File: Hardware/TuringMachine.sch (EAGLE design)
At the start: 79 parts, among them IC1 TL072, IC2 4015, IC3 4015, IC4 TL074, IC5 4016, T1 2N3904, T2 2N3904, T3 2N3904

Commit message: Hand routing
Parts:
- removed 78L09: (no value), v-reg:78LXX
- removed IC4: TL074, linear:TL074P
- added C17: 1n, TomW:C-EU050-024X044
- added C18: 0.47uf, rcl:C-EU050-035X075
- added IC6, IC7: TL072P, TomW:TL072P
- added R20: 3.3k, TomW:R-EU_0207/7
- added TL431: (no value), TomW:TL431CLP
- C12: value 100n -> 1n
- IC1: value TL072 -> TL072P
- R26: value 10k -> 5.1k
- R27, R28: value 10k -> 1.6k
- R3: value 100k -> 68k
- R7: value 1m -> 470k
- renumbered ADD_0_1 to WRITE
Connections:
- removed net N$38: 78L09.OUT, R28.1
- new net N$18: R20.1, R28.1, TL431.C, TL431.R
- new net N$9: C18.1, R32.1
- net +12V: now also IC6P.V+, IC7P.V+, R1.1, R20.2, R23.1; no longer 78L09.IN, C12.1, IC4P.V+, R1.2, R23.2
- net -12V: now also IC6P.V-, IC7P.V-, R35.1; no longer IC4P.V-, R35.2
- net B1: now also R14.2; no longer R14.1
- net END_OF_LOOP: now also IC5A.A, R4.1; no longer IC5D.A, R4.2
- net GND: now also C1.1, C15.1, C3.1, IC5C.C, IC5D.C, IC6A.+IN, IC7A.+IN, R27.1, TL431.A; no longer 78L09.GND, C1.2, C12.2, C15.2, C3.2, IC4A.+IN, IC4C.+IN, IC5A.C, IC5B.C, R27.2
- net MAIN_OUT: now also C17.2, IC7A.OUT; no longer IC4A.OUT
- net N$1: now also R4.2; no longer R4.1
- net N$10: now also C1.2; no longer C1.1
- net N$11: now also R18.1; no longer R18.2
- net N$12: now also IC7B.-IN; no longer IC4B.-IN
- net N$13: now also C17.1, IC7A.-IN; no longer IC4A.-IN
- net N$16: now also C10.1; no longer C10.2
- net N$19: now also R18.2; no longer R18.1
- net N$20: now also C10.2, R30.1; no longer C10.1, R30.2
- net N$21: now also R30.2, R31.2; no longer R30.1, R31.1
- net N$22: now also C18.2, R31.1; no longer R31.2, R32.2
- net N$23: now also R27.2; no longer R27.1
- net N$24: now also IC5A.C, IC6B.OUT, R25.1; no longer IC4D.OUT, IC5D.C, R25.2
- net N$27: now also C12.1, R32.2; no longer R32.1
- net N$28: now also R14.1; no longer R14.2
- net N$4: now also IC5B.A, R1.2; no longer IC5C.A, R1.1
- net N$41: now also C11.1, C12.2; no longer C11.2
- net N$44: now also R25.2; no longer R25.1
- net N$45: now also IC5B.C; no longer IC5C.C
- net N$47: now also R23.2; no longer R23.1
- net N$48: now also R35.2; no longer R35.1
- net N$5: now also C15.2, IC7B.+IN; no longer C15.1, IC4B.+IN
- net N$6: now also IC6A.-IN; no longer IC4C.-IN
- net N$7: now also IC6A.OUT, IC6B.-IN; no longer IC4C.OUT, IC4D.-IN
- net N$8: now also IC7B.OUT; no longer IC4B.OUT
- net NOISE: now also C11.2, IC6B.+IN; no longer C11.1, IC4D.+IN
- net START_OF_LOOP: now also IC5A.B, IC5B.B; no longer IC5C.B, IC5D.B
- net STEP_12: now also C3.2; no longer C3.1
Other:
- moved on the sheet: C10, C12, C13, C14, C5, C6, C7, C8, EXPANSION, IC1A, IC2P, IC3P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

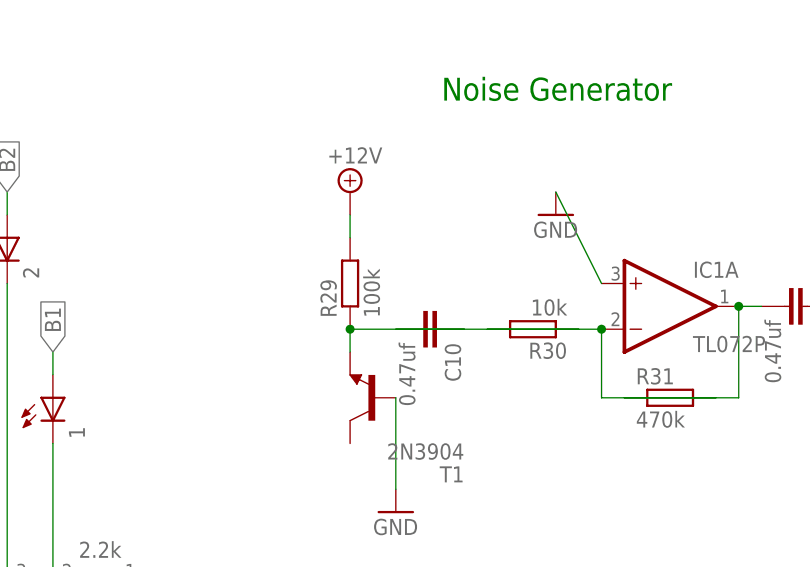
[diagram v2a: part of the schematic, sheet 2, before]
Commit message: manual routing
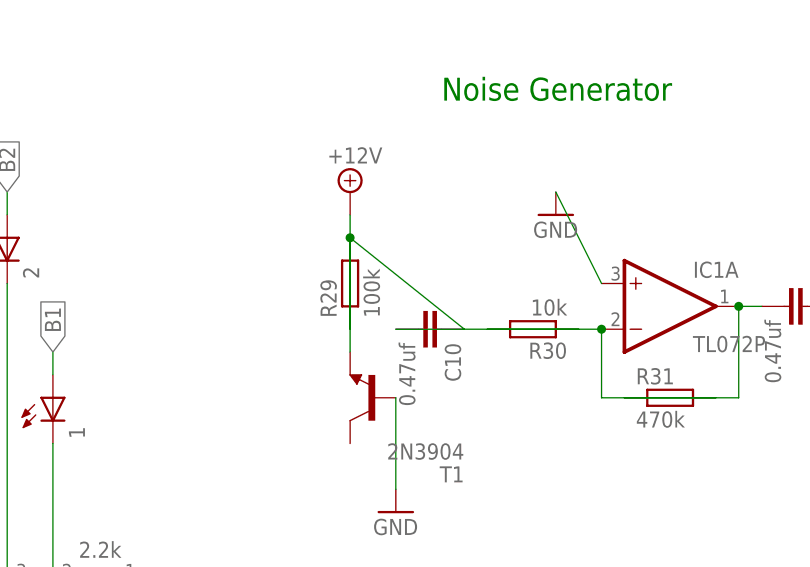
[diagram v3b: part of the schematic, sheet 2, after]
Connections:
- net +12V: now also R29.1; no longer R29.2
- net N$16: now also R29.2; no longer R29.1
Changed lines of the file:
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@@
 </segment>
 <segment>
-<pinref part="R29" gate="G$1" pin="2"/>
+<pinref part="R29" gate="G$1" pin="1"/>
 <pinref part="P+13" gate="+12V" pin="+12V"/>
-<wire x1="142.24" y1="91.44" x2="142.24" y2="88.9" width="0.1524" layer="91"/>
+<wire x1="142.24" y1="91.44" x2="142.24" y2="78.74" width="0.1524" layer="91"/>
 </segment>
 <segment>
@@
 <segment>
 <pinref part="T1" gate="G1" pin="E"/>
-<pinref part="R29" gate="G$1" pin="1"/>
-<wire x1="142.24" y1="76.2" x2="142.24" y2="78.74" width="0.1524" layer="91"/>
+<pinref part="R29" gate="G$1" pin="2"/>
+<wire x1="142.24" y1="76.2" x2="142.24" y2="88.9" width="0.1524" layer="91"/>
 <pinref part="C10" gate="G$1" pin="1"/>
-<wire x1="154.94" y1="78.74" x2="142.24" y2="78.74" width="0.1524" layer="91"/>
-<junction x="142.24" y="78.74"/>
-</segment>
-</net>
+<wire x1="154.94" y1="78.74" x2="142.24" y2="88.9" width="0.1524" layer="91"/>
+<junction x="142.24" y="88.9"/>
+</segment>
+</net>

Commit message: routing
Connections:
- net GND: now also C16.2, R9.2; no longer C16.1, R9.1
- net N$12: now also C16.1, R9.1; no longer C16.2, R9.2
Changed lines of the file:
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@@
 <?xml version="1.0" encoding="utf-8"?>
 <!DOCTYPE eagle SYSTEM "eagle.dtd">
-<eagle version="7.2.0">
+<eagle version="6.6.0">
 <drawing>
 <settings>
@@
 </segment>
 <segment>
-<pinref part="R9" gate="G$1" pin="1"/>
+<pinref part="R9" gate="G$1" pin="2"/>
 <pinref part="GND2" gate="1" pin="GND"/>
 <wire x1="330.2" y1="48.26" x2="330.2" y2="50.8" width="0.1524" layer="91"/>
-<wire x1="330.2" y1="50.8" x2="330.2" y2="53.34" width="0.1524" layer="91"/>
+<wire x1="330.2" y1="50.8" x2="330.2" y2="63.5" width="0.1524" layer="91"/>
 <wire x1="330.2" y1="50.8" x2="345.44" y2="50.8" width="0.1524" layer="91"/>
 <junction x="330.2" y="50.8"/>
-<pinref part="C16" gate="G$1" pin="1"/>
-<wire x1="345.44" y1="50.8" x2="345.44" y2="55.88" width="0.1524" layer="91"/>
+<pinref part="C16" gate="G$1" pin="2"/>
+<wire x1="345.44" y1="50.8" x2="345.44" y2="63.5" width="0.1524" layer="91"/>
 </segment>
 <segment>
@@
 <net name="N$12" class="0">
 <segment>
-<pinref part="R9" gate="G$1" pin="2"/>
+<pinref part="R9" gate="G$1" pin="1"/>
 <pinref part="R3" gate="G$1" pin="1"/>
 <wire x1="330.2" y1="86.36" x2="330.2" y2="71.12" width="0.1524" layer="91"/>
 <pinref part="IC7" gate="B" pin="-IN"/>
 <wire x1="330.2" y1="71.12" x2="330.2" y2="66.04" width="0.1524" layer="91"/>
-<wire x1="330.2" y1="66.04" x2="330.2" y2="63.5" width="0.1524" layer="91"/>
+<wire x1="330.2" y1="66.04" x2="330.2" y2="53.34" width="0.1524" layer="91"/>
 <wire x1="332.74" y1="71.12" x2="330.2" y2="71.12" width="0.1524" layer="91"/>
 <junction x="330.2" y="71.12"/>
 <wire x1="330.2" y1="66.04" x2="345.44" y2="66.04" width="0.1524" layer="91"/>
 <junction x="330.2" y="66.04"/>
-<pinref part="C16" gate="G$1" pin="2"/>
-<wire x1="345.44" y1="66.04" x2="345.44" y2="63.5" width="0.1524" layer="91"/>
-</segment>
-</net>
+<pinref part="C16" gate="G$1" pin="1"/>
+<wire x1="345.44" y1="66.04" x2="345.44" y2="55.88" width="0.1524" layer="91"/>
+</segment>
+</net>

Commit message: routing
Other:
- moved on the sheet: C1, C10, C11, C12, C15, C16, C17, C3, R1, R14, R18, R23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

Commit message: Prototype 1 complete and sent to OSHPark
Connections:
- net N$22: now also C18.1; no longer C18.2
- net N$9: now also C18.2; no longer C18.1
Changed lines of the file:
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@@
 <wire x1="185.42" y1="71.12" x2="185.42" y2="81.28" width="0.1524" layer="91"/>
 <pinref part="IC1" gate="A" pin="OUT"/>
-<pinref part="C18" gate="G$1" pin="2"/>
-<wire x1="187.96" y1="81.28" x2="185.42" y2="81.28" width="0.1524" layer="91"/>
+<pinref part="C18" gate="G$1" pin="1"/>
+<wire x1="195.58" y1="81.28" x2="185.42" y2="81.28" width="0.1524" layer="91"/>
 <junction x="185.42" y="81.28"/>
 </segment>
@@
 <net name="N$9" class="0">
 <segment>
-<pinref part="C18" gate="G$1" pin="1"/>
+<pinref part="C18" gate="G$1" pin="2"/>
 <pinref part="R32" gate="G$1" pin="1"/>
-<wire x1="195.58" y1="81.28" x2="198.12" y2="81.28" width="0.1524" layer="91"/>
-</segment>
-</net>
+<wire x1="187.96" y1="81.28" x2="198.12" y2="81.28" width="0.1524" layer="91"/>
+</segment>
+</net>

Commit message: Added BOM
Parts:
- R5: value 50k -> 51k
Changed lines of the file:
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@@
 <part name="P+1" library="supply2" deviceset="+12V" device=""/>
 <part name="CV_IN" library="MusicThingModular" deviceset="THONKICONN" device=""/>
-<part name="R5" library="TomW" deviceset="R-EU_" device="0207/7" value="50k"/>
+<part name="R5" library="TomW" deviceset="R-EU_" device="0207/7" value="51k"/>
 <part name="GND16" library="supply1" deviceset="GND" device=""/>
 <part name="R6" library="TomW" deviceset="R-EU_" device="0207/7" value="150k"/>

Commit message: Update R32 in noise and R6 in CV input
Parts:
- R32: value 10k -> 1k
- R6: value 150k -> 47k
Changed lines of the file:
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@@
 <part name="GND27" library="supply1" deviceset="GND" device=""/>
 <part name="R31" library="TomW" deviceset="R-EU_" device="0207/7" value="470k"/>
-<part name="R32" library="TomW" deviceset="R-EU_" device="0207/7" value="10k"/>
+<part name="R32" library="TomW" deviceset="R-EU_" device="0207/7" value="1k"/>
 <part name="GND28" library="supply1" deviceset="GND" device=""/>
 <part name="NOISE-OUT" library="MusicThingModular" deviceset="THONKICONN" device=""/>
@@
 <part name="R5" library="TomW" deviceset="R-EU_" device="0207/7" value="51k"/>
 <part name="GND16" library="supply1" deviceset="GND" device=""/>
-<part name="R6" library="TomW" deviceset="R-EU_" device="0207/7" value="150k"/>
+<part name="R6" library="TomW" deviceset="R-EU_" device="0207/7" value="47k"/>
 <part name="GND19" library="supply1" deviceset="GND" device=""/>
 <part name="CV_OUT" library="MusicThingModular" deviceset="THONKICONN" device=""/>
